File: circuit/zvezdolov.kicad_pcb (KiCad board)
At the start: 2 copper layers, 86.4 x 132.1 mm, 45 parts, among them IC1 ATTINY84A-P, IC2 DM13A, IC3 TLC5943, P1 PWR, P2 ROTENC, P3 ICSP, P4 RGB, Q1 BS170, SW1 SW_RESET, U1 LE33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

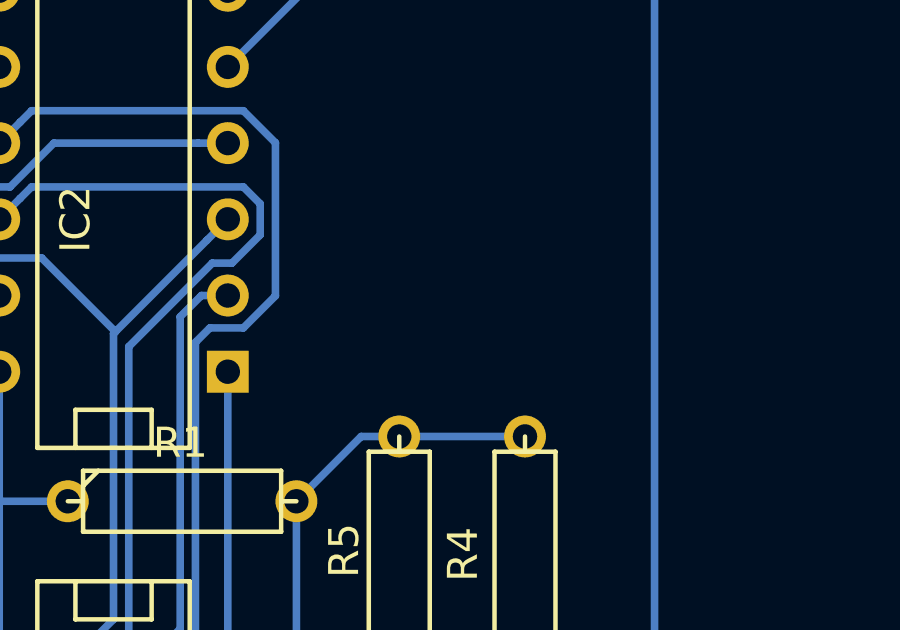
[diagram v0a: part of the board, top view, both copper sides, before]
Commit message: Add a debounce capacitor to the encoder.
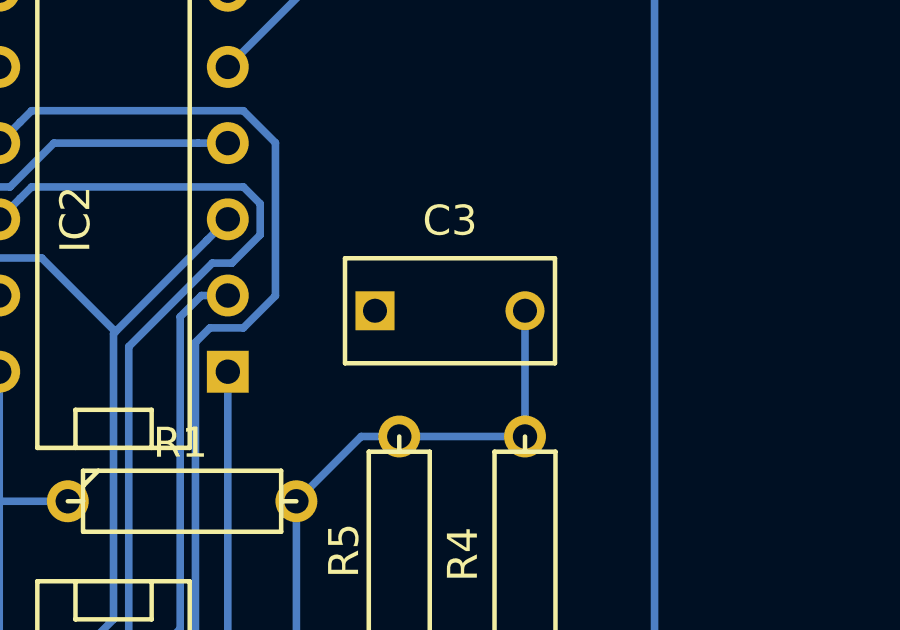
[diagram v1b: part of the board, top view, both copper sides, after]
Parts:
- added C3: 10n, Capacitors_ThroughHole:C_Rect_L7_W3.5_P5, F.Cu at (148.4, 90.0)
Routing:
- net Net-(C3-Pad2): track 23.3 -> 27.5 mm

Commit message: PCB text tweaks.
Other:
- board text removed: "June 2015"
- board text removed: "Zvezdolov Poly-Color Brilliance"

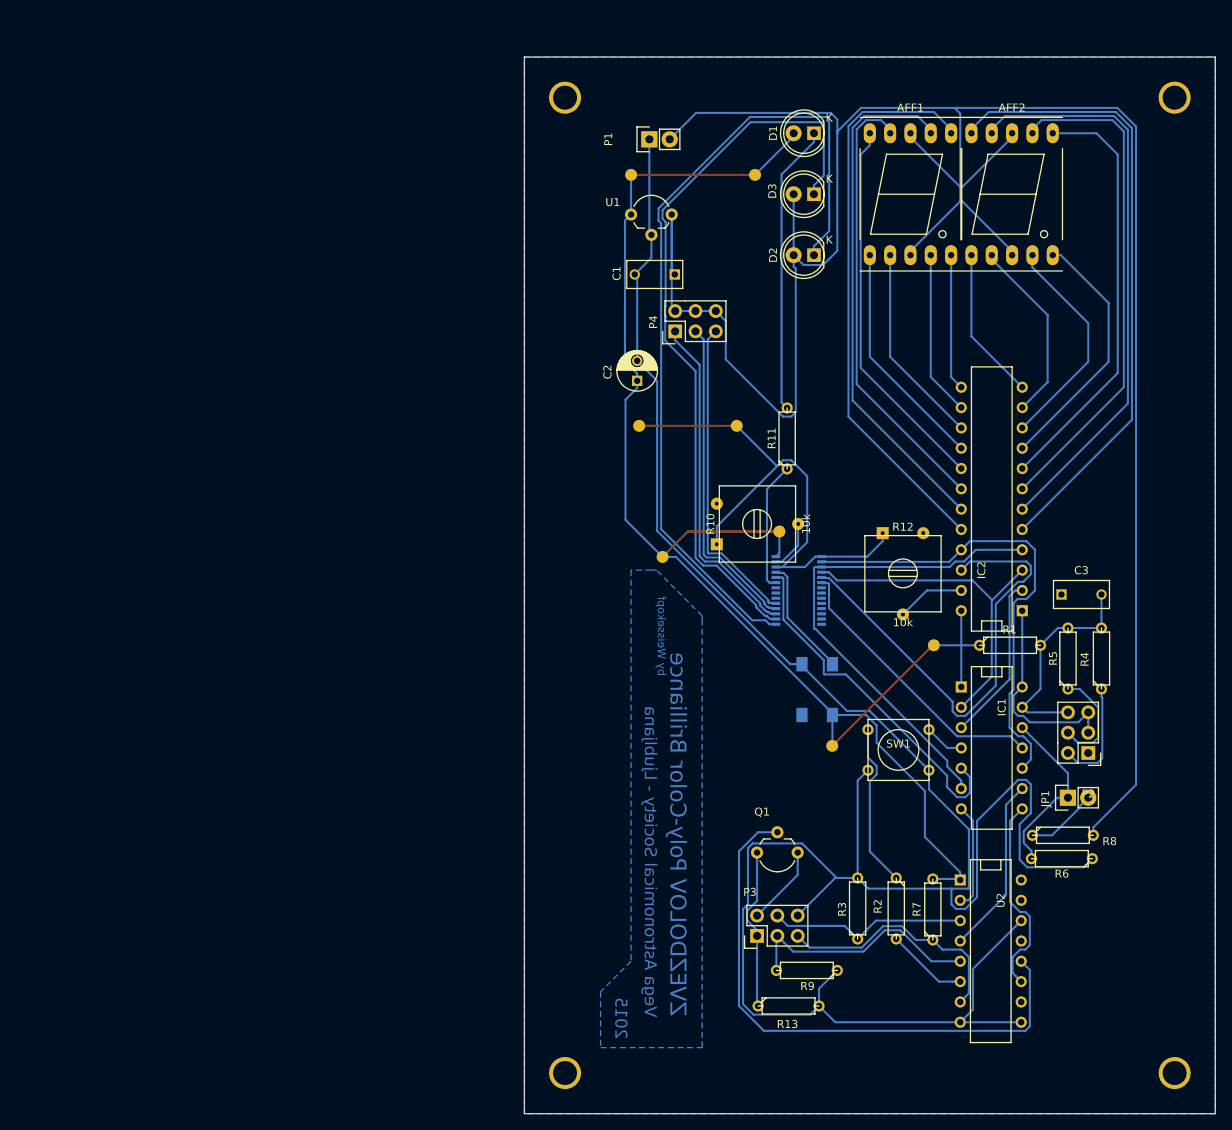
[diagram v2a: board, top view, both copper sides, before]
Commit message: Make the PCB considerably smaller.
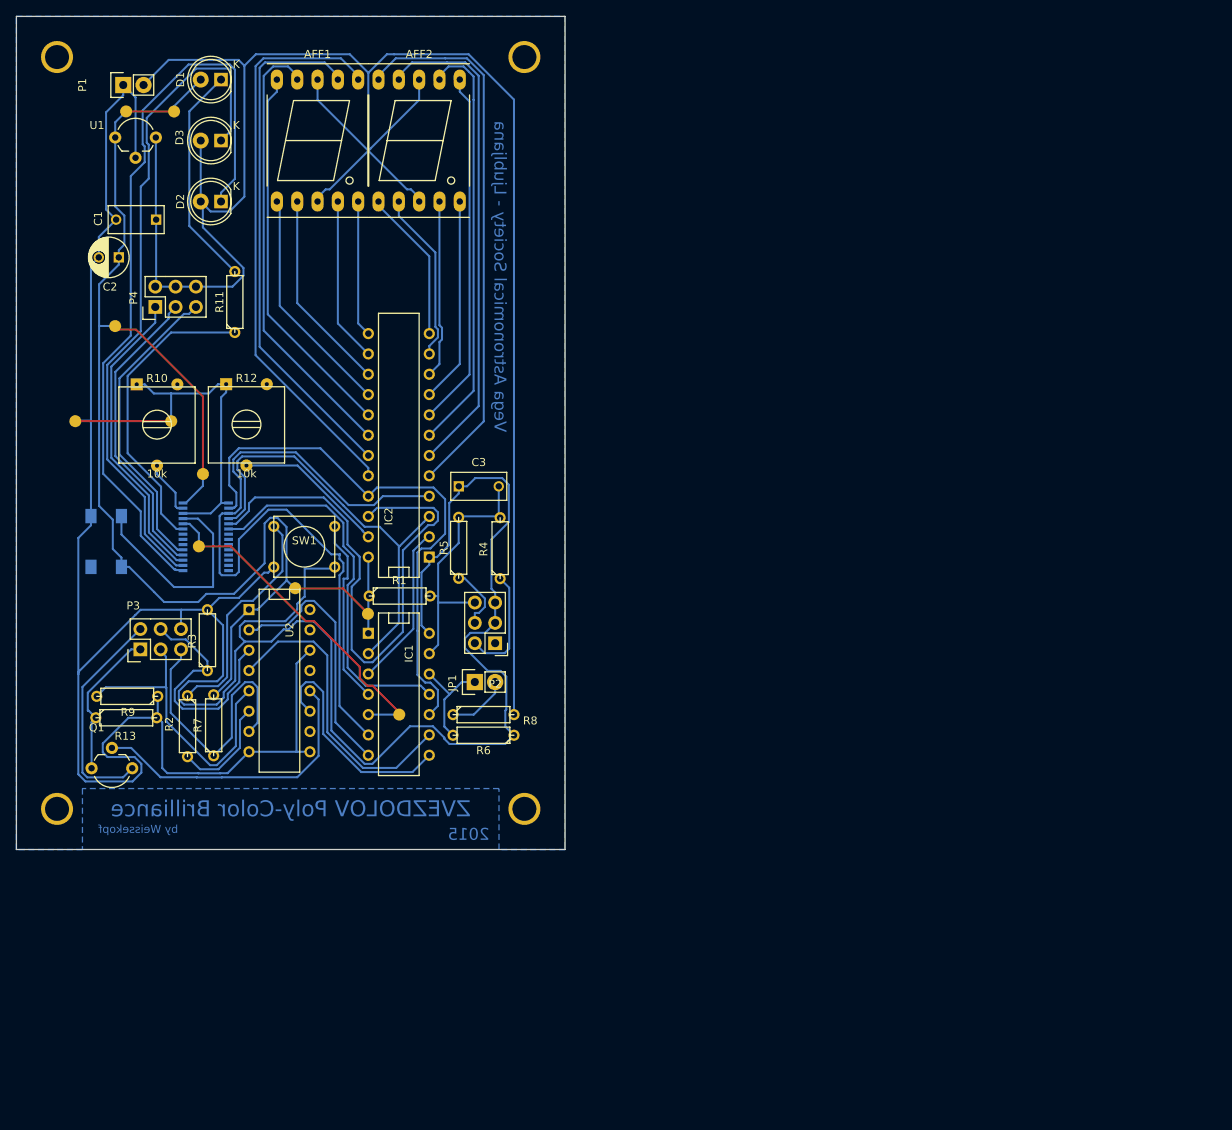
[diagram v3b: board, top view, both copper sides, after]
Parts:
- removed the ? at (95.6, 69.0)
- removed the ? at (107.8, 69.0)
- removed the ? at (98.6, 85.3)
- removed the ? at (113.2, 82.2)
- removed the ? at (119.8, 109.0)
- removed the ? at (132.5, 96.4)
- removed the ? at (94.6, 37.6)
- removed the ? at (110.1, 37.6)
- added ?: , zvezdolov:GPAD, F.Cu at (25.1, 68.4)
- added ?: , zvezdolov:GPAD, F.Cu at (37.5, 29.7)
- added ?: , zvezdolov:GPAD, F.Cu at (37.1, 68.4)
- added ?: , zvezdolov:GPAD, F.Cu at (30.1, 56.5)
- added ?: , zvezdolov:GPAD, F.Cu at (41.1, 75.0)
- added ?: , zvezdolov:GPAD, F.Cu at (40.6, 84.0)
- added ?: , zvezdolov:GPAD, F.Cu at (65.6, 105.1)
- added ?: , zvezdolov:GPAD, F.Cu at (52.6, 89.3)
- added ?: , zvezdolov:GPAD, F.Cu at (61.7, 92.5)
- added ?: , zvezdolov:GPAD, F.Cu at (31.5, 29.7)
- moved U2 95.1 mm to (50.7, 100.8)
- moved R7 92.8 mm to (42.4, 106.4)
- moved R9 91.6 mm to (31.6, 102.8)
- moved R2 91.5 mm to (39.2, 106.5)
- moved O1 90.8 mm to (29.0, 83.4)
- moved R13 90.3 mm to (31.5, 105.5)
- moved R3 87.9 mm to (41.7, 95.8)
- moved MOUNT3 87.7 mm to (81.3, 116.8)
- moved P3 85.0 mm to (33.3, 96.9)
- moved R12 84.1 mm to (44.0, 68.8)
- moved Q1 83.9 mm to (32.3, 111.8)
- moved MOUNT2 81.4 mm to (81.3, 22.9)
- moved R10 79.0 mm to (32.8, 68.9), turned to 0 degrees
- moved SW1 78.5 mm to (53.8, 84.1)
- moved R5 77.4 mm to (73.1, 84.2)
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- gave numbers to parts that had none: 4
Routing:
- net +9V: track 297.9 -> 256.5 mm
- net GND: track 382.0 -> 420.4 mm
- net Net-(Q1-Pad2): track 71.6 -> 37.1 mm
- net /LAT: track 62.2 -> 92.4 mm
- net Net-(IC1-Pad4): track 25.7 -> 52.3 mm
- net Net-(IC3-Pad23): track 16.2 -> 38.1 mm
- net /MOSI: track 13.3 -> 32.1 mm
- net Net-(P3-Pad2): track 9.98 -> 28.3 mm
- net /SCK: track 22.3 -> 37.9 mm
- net Net-(IC3-Pad25): track 15.0 -> 27.7 mm
- net /SIN: track 57.8 -> 70.3 mm
- net VCC: track 193.3 -> 180.8 mm
- net /BCSEL: track 35.4 -> 47.0 mm
- net /USCK: track 43.1 -> 54.4 mm
- net Net-(IC2-Pad23): track 8.53 -> 19.0 mm
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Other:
- board size 86.4 x 132.1 mm -> 68.6 x 104.1 mm

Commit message: Fix texts, add logos and bump PCB revision.
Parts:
- added REF**: winkey, winkey, F.Cu at (28.6, 119.4)
- added REF**: Symbol_GNU-Logo_CopperTop, Symbols:Symbol_GNU-Logo_CopperTop, B.Cu at (26.3, 93.1)
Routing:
- net GND: track 420.4 -> 414.6 mm
- net Net-(P3-Pad2): track 28.3 -> 29.3 mm
- net Net-(P3-Pad1): track 19.0 -> 19.5 mm
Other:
- board text added: "Astronomical Society Vega - Ljubljana"
- board text removed: "Vega Astronomical Society - Ljubljana"

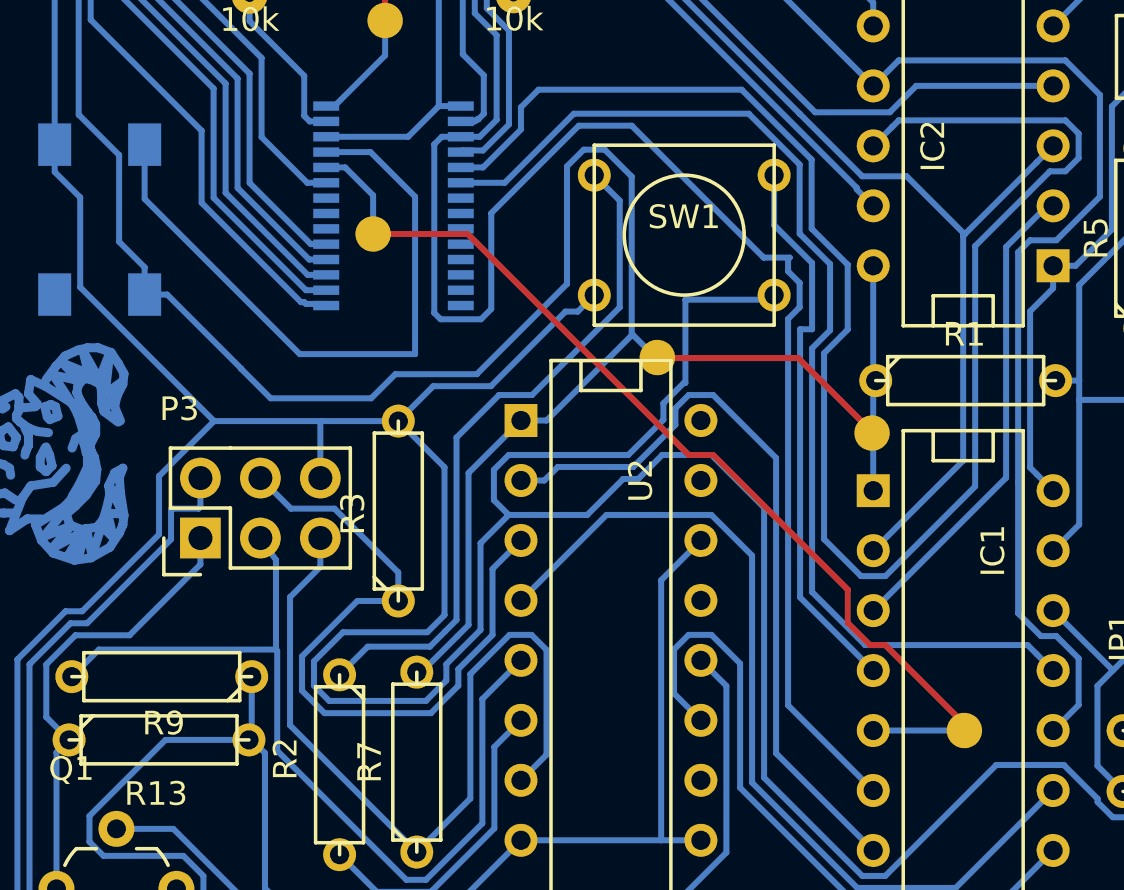
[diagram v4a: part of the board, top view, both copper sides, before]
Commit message: Move a wire pad from under IC3 where it was in the way.
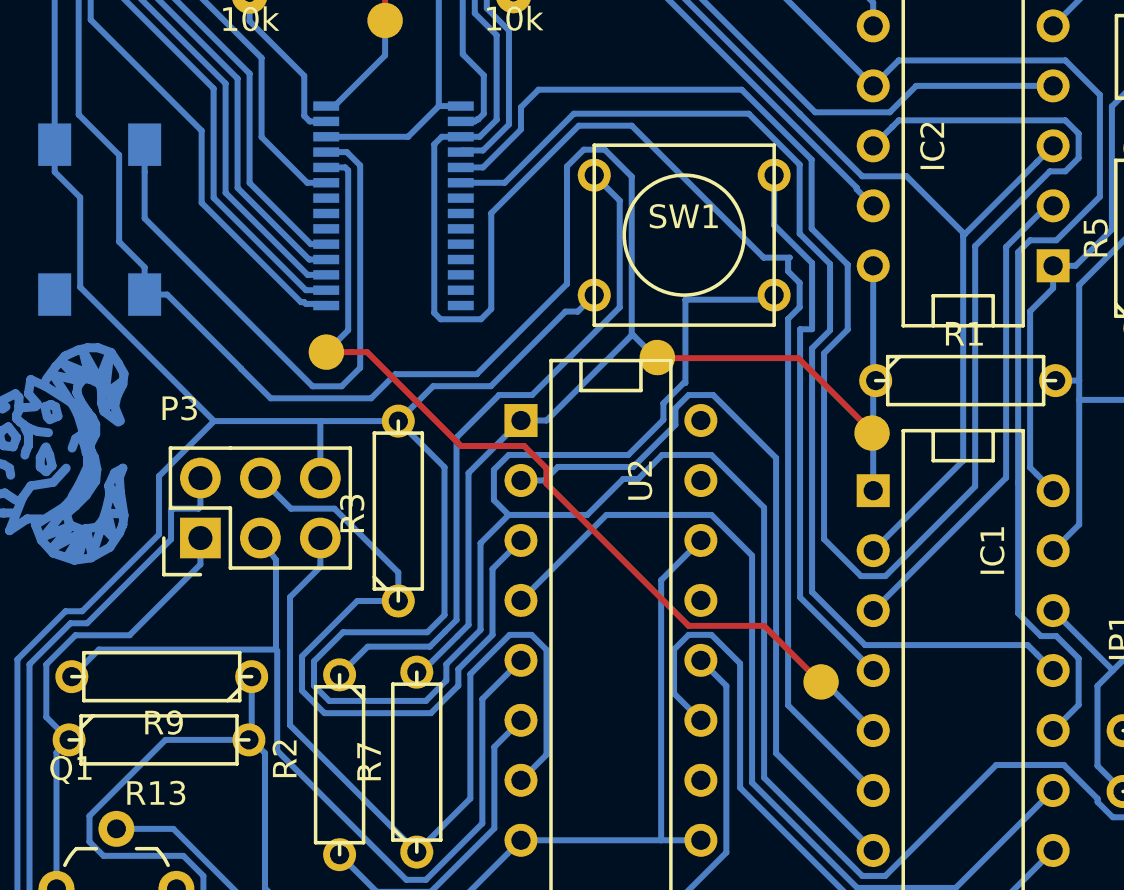
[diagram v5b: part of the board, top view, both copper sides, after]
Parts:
- moved ? 128.9 mm to (-6.07, -2.06)
- moved ? 5.38 mm to (38.6, 89.0)
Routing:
- net /DI: track 42.7 -> 39.4 mm
- net Net-(IC3-Pad25): track 27.7 -> 25.8 mm
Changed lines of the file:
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@@
     (links 117)
     (no_connects 1)
-    (area 5.549014 17.6805 270.104286 194.24)
+    (area 5.549014 17.6805 270.104286 209.0554)
     (thickness 1.6)
     (drawings 9)
-    (tracks 711)
+    (tracks 717)
     (zones 0)
     (modules 50)
@@
   (title_block
     (title "Zvezdolov Poly-Color Brilliance")
-    (date "June 2015")
-    (rev 5)
+    (date "July 2015")
+    (rev 6)
     (company "Astronomical Society Vega - Ljubljana")
   )
@@
   )
   (module zvezdolov:GPAD (layer F.Cu)
-    (at 40.5892 84.0232)
+    (at 38.608 89.027)
     (fp_text reference "" (at 0 0.75) (layer F.SilkS) hide
       (effects (font (size 1.5 1.5) (thickness 0.15)))
@@
   )
   (module zvezdolov:GPAD (layer F.Cu)
-    (at 65.6336 105.0544)
+    (at -6.0706 -2.0574)
     (fp_text reference "" (at 0 0.75) (layer F.SilkS) hide
       (effects (font (size 1.5 1.5) (thickness 0.15)))
@@
       (effects (font (size 1.5 1.5) (thickness 0.15)))
     )
-    (pad "" smd circle (at 0 0) (size 1.5 1.5) (layers *.Cu F.Paste F.Mask)
+    (pad "" smd circle (at 65.6336 105.0544) (size 1.5 1.5) (layers *.Cu F.Paste F.Mask)
       (net 33 /DI))
   )
@@
   (segment (start 37.7988 81.8544) (end 35.86485 79.92045) (width 0.254) (layer B.Cu) (net 32))
   (segment (start 35.86485 76.566602) (end 31.680799 72.382551) (width 0.254) (layer B.Cu) (net 32))
-  (via (at 40.5892 84.0232) (size 0.889) (layers F.Cu B.Cu) (net 33))
-  (segment (start 40.5892 82.3868) (end 40.5892 84.0232) (width 0.254) (layer B.Cu) (net 33))
-  (segment (start 39.4068 81.2044) (end 40.5892 82.3868) (width 0.254) (layer B.Cu) (net 33))
-  (segment (start 38.6028 81.2044) (end 39.4068 81.2044) (width 0.254) (layer B.Cu) (net 33) (status 10))
-  (via (at 65.6336 105.0544) (size 0.889) (layers F.Cu B.Cu) (net 33))
-  (segment (start 65.6336 104.777538) (end 65.6336 105.0544) (width 0.254) (layer F.Cu) (net 33))
-  (segment (start 62.290961 101.434899) (end 65.6336 104.777538) (width 0.254) (layer F.Cu) (net 33))
-  (segment (start 61.635637 101.434899) (end 62.290961 101.434899) (width 0.254) (layer F.Cu) (net 33))
-  (segment (start 60.693299 100.492561) (end 61.635637 101.434899) (width 0.254) (layer F.Cu) (net 33))
-  (segment (start 60.693299 99.086237) (end 60.693299 100.492561) (width 0.254) (layer F.Cu) (net 33))
-  (segment (start 54.990961 93.383899) (end 60.693299 99.086237) (width 0.254) (layer F.Cu) (net 33))
-  (segment (start 53.954639 93.383899) (end 54.990961 93.383899) (width 0.254) (layer F.Cu) (net 33))
-  (segment (start 44.59394 84.0232) (end 53.954639 93.383899) (width 0.254) (layer F.Cu) (net 33))
-  (segment (start 40.5892 84.0232) (end 44.59394 84.0232) (width 0.254) (layer F.Cu) (net 33))
-  (segment (start 65.6336 105.0544) (end 61.7728 105.0544) (width 0.254) (layer B.Cu) (net 33) (status 20))
+  (segment (start 59.563 103.0351) (end 59.563 102.997) (width 0.254) (layer B.Cu) (net 33))
+  (via (at 38.608 89.027) (size 0.889) (drill 0) (layers F.Cu B.Cu) (net 33))
+  (segment (start 39.4068 81.2044) (end 38.6028 81.2044) (width 0.254) (layer B.Cu) (net 33))
+  (segment (start 39.533801 81.331401) (end 39.4068 81.2044) (width 0.254) (layer B.Cu) (net 33))
+  (segment (start 39.533801 88.101199) (end 39.533801 81.331401) (width 0.254) (layer B.Cu) (net 33))
+  (segment (start 38.608 89.027) (end 39.533801 88.101199) (width 0.254) (layer B.Cu) (net 33))
+  (segment (start 59.7154 102.997) (end 59.563 102.997) (width 0.254) (layer B.Cu) (net 33))
+  (via (at 59.563 103.0351) (size 0.889) (drill 0) (layers F.Cu B.Cu) (net 33))
+  (segment (start 59.7535 103.0351) (end 59.563 103.0351) (width 0.254) (layer B.Cu) (net 33))
+  (segment (start 61.7728 105.0544) (end 59.7535 103.0351) (width 0.254) (layer B.Cu) (net 33))
+  (segment (start 39.66866 89.027) (end 38.608 89.027) (width 0.254) (layer F.Cu) (net 33))
+  (segment (start 40.332662 89.027) (end 39.66866 89.027) (width 0.254) (layer F.Cu) (net 33))
+  (segment (start 46.989963 93.002901) (end 44.308563 93.002901) (width 0.254) (layer F.Cu) (net 33))
+  (segment (start 47.932301 93.945239) (end 46.989963 93.002901) (width 0.254) (layer F.Cu) (net 33))
+  (segment (start 47.932301 94.600563) (end 47.932301 93.945239) (width 0.254) (layer F.Cu) (net 33))
+  (segment (start 44.308563 93.002901) (end 40.332662 89.027) (width 0.254) (layer F.Cu) (net 33))
+  (segment (start 53.954639 100.622901) (end 47.932301 94.600563) (width 0.254) (layer F.Cu) (net 33))
+  (segment (start 57.150801 100.622901) (end 53.954639 100.622901) (width 0.254) (layer F.Cu) (net 33))
+  (segment (start 59.563 103.0351) (end 57.150801 100.622901) (width 0.254) (layer F.Cu) (net 33))
   (segment (start 35.3568 73.9394) (end 35.3568 75.007131) (width 0.254) (layer B.Cu) (net 34) (status 10))
   (segment (start 35.3568 75.007131) (end 37.671799 77.32213) (width 0.254) (layer B.Cu) (net 34))
@@
   (segment (start 71.2708 103.1644) (end 71.2708 106.5524) (width 0.254) (layer B.Cu) (net 38))
   (segment (start 71.9268 102.5084) (end 71.2708 103.1644) (width 0.254) (layer B.Cu) (net 38))
-  (segment (start 40.480434 80.5544) (end 38.6028 80.5544) (width 0.254) (layer B.Cu) (net 39) (status 20))
-  (segment (start 42.3672 82.441166) (end 40.480434 80.5544) (width 0.254) (layer B.Cu) (net 39))
-  (segment (start 42.3672 89.110424) (end 42.3672 82.441166) (width 0.254) (layer B.Cu) (net 39))
-  (segment (start 37.483156 89.110424) (end 42.3672 89.110424) (width 0.254) (layer B.Cu) (net 39))
-  (segment (start 30.9118 82.539068) (end 37.483156 89.110424) (width 0.254) (layer B.Cu) (net 39))
-  (segment (start 30.9118 80.2386) (end 30.9118 82.539068) (width 0.254) (layer B.Cu) (net 39) (status 10))
+  (segment (start 30.9118 81.39303) (end 30.9118 80.2386) (width 0.254) (layer B.Cu) (net 39))
+  (segment (start 30.9118 83.3628) (end 30.9118 81.39303) (width 0.254) (layer B.Cu) (net 39))
+  (segment (start 38.023819 90.474819) (end 30.9118 83.3628) (width 0.254) (layer B.Cu) (net 39))
+  (segment (start 39.255681 90.474819) (end 38.023819 90.474819) (width 0.254) (layer B.Cu) (net 39))
+  (segment (start 40.041811 89.688689) (end 39.255681 90.474819) (width 0.254) (layer B.Cu) (net 39))
+  (segment (start 40.041811 81.120977) (end 40.041811 89.688689) (width 0.254) (layer B.Cu) (net 39))
+  (segment (start 39.475234 80.5544) (end 40.041811 81.120977) (width 0.254) (layer B.Cu) (net 39))
+  (segment (start 38.6028 80.5544) (end 39.475234 80.5544) (width 0.254) (layer B.Cu) (net 39))
   (segment (start 76.329401 97.375001) (end 75.0848 96.1304) (width 0.254) (layer B.Cu) (net 40) (status 20))
   (segment (start 78.793201 97.375001) (end 76.329401 97.375001) (width 0.254) (layer B.Cu) (net 40))

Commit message: Fix the broken ICSP setup.
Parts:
- removed Q1: BS170, Housings_TO-92:TO-92_Molded_Wide_Reverse
- removed R13: 10k, Discret:R3
- moved R9 3.23 mm to (34.4, 104.5), turned to 90 degrees
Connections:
- net GND renamed VSS
- P3 pad 2: Net-(P3-Pad2) -> (no net)
- U2 pad 12: Net-(Q1-Pad2) -> Net-(P3-Pad1)
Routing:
- net VSS: track 414.6 -> 294.1 mm, vias 2 -> 0
- net Net-(Q1-Pad2): track 37.1 -> 0.00 mm
- net Net-(P3-Pad2): track 29.3 -> 0.00 mm
- net Net-(P3-Pad1): track 19.5 -> 45.6 mm
- net Net-(P3-Pad3): track 37.9 -> 30.9 mm
